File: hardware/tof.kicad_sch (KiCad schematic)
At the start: 0 parts

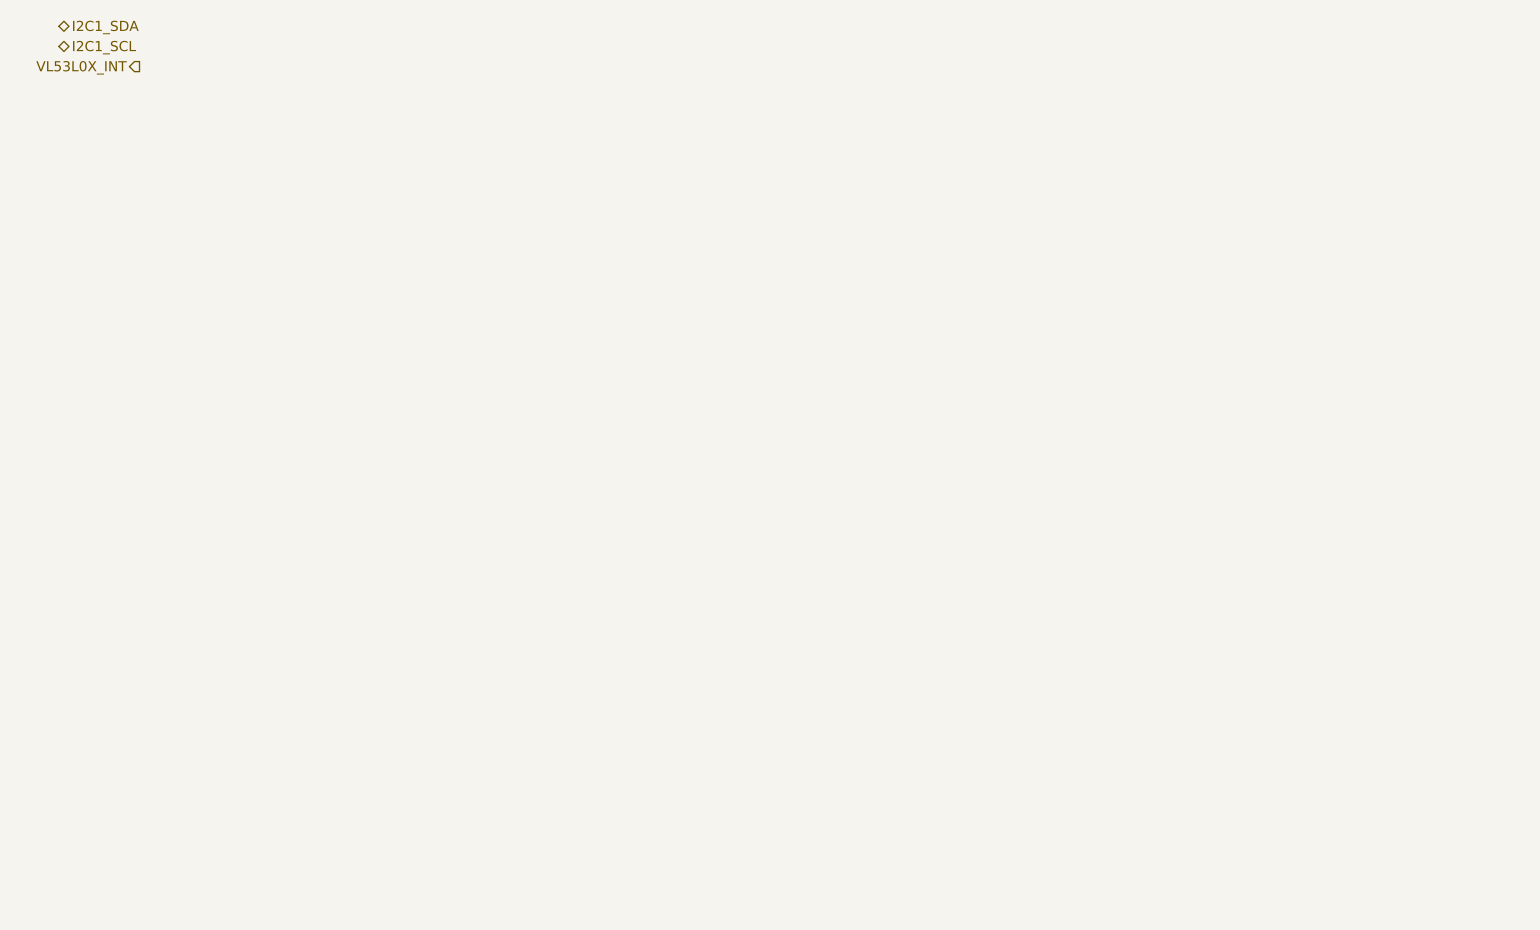
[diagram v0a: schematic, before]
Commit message: feat(kicad): Added several open sourced footprint libraries, finished schematic design for nrf, uwb, tof, flash, motors and added all reference material to refs folder
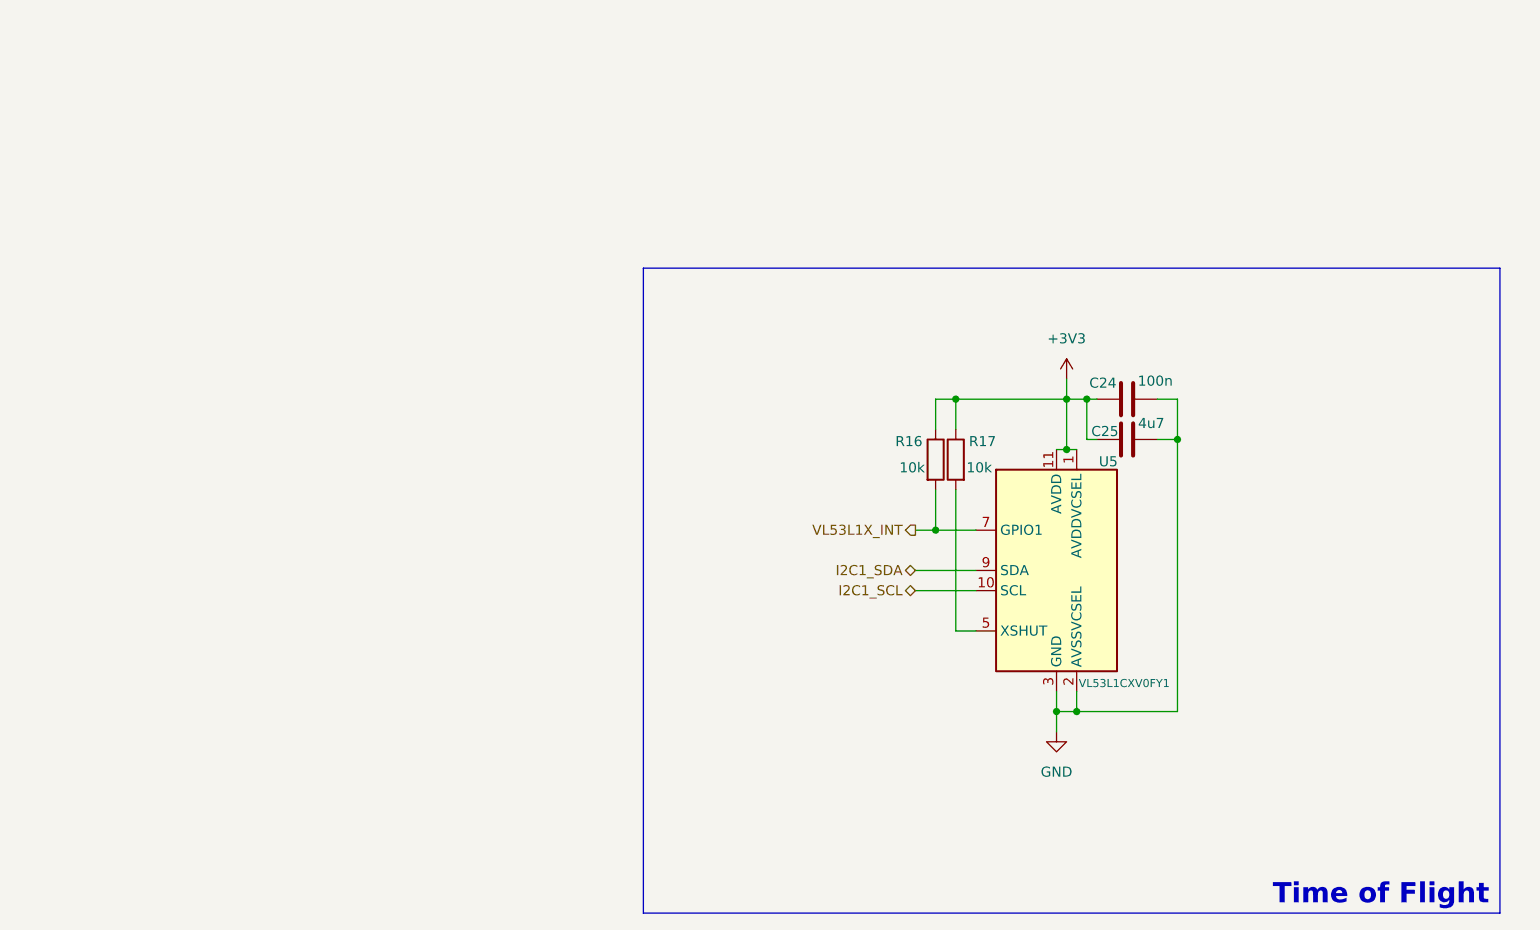
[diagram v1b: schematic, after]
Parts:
- added C24: 100n, symbol Device:C
- added C25: 4u7, symbol Device:C
- added R16, R17: 10k, symbol Device:R
- added U5: VL53L1CXV0FY1, Sensor_Distance:ST_VL53L1x, symbol Sensor_Distance:VL53L1CXV0FY1
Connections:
- net I2C1_SCL: now also U5.10 (SCL)
- net I2C1_SDA: now also U5.9 (SDA)
- new net: R17.2, U5.5 (XSHUT)
- new net +3V3: C24.1, C25.1, R16.1, R17.1, U5.1 (AVDDVCSEL), U5.11 (AVDD)
- new net GND: C24.2, C25.2, U5.12 (GND), U5.2 (AVSSVCSEL), U5.3 (GND), U5.4 (GND), U5.6 (GND)
- new net VL53L1X_INT: R16.2, U5.7 (GPIO1)
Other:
- note added: "Time of Flight"
